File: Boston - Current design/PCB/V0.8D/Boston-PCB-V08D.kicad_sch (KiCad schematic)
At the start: 596 parts, among them J701 Conn_01x04_MountingPin, J702 Conn_01x03, J705 Conn_01x04_MountingPin, J706 Conn_ARM_JTAG_SWD_10, Q701 DTC123J, Q702 AO4406AL, SW1 MXSwitch, SW10 MXSwitch, SW100 MXSwitch, SW101 MXSwitch, SW102 MXSwitch, SW103 MXSwitch, SW104 MXSwitch, SW105-1 MXSwitch, SW105-2 MXSwitch, SW106 MXSwitch, SW107 MXSwitch, SW108 MXSwitch, SW109 MXSwitch, SW11 MXSwitch, SW110 MXSwitch, SW111 MXSwitch, SW112 MXSwitch, SW113 MXSwitch, SW114 MXSwitch, SW115 MXSwitch, SW116 MXSwitch, SW117 MXSwitch, SW118 MXSwitch, SW119 MXSwitch, SW12 MXSwitch, SW120 MXSwitch, SW121 MXSwitch, SW122 MXSwitch, SW123 MXSwitch, SW124-1 MXSwitch, SW124-2 MXSwitch, SW125 MXSwitch, SW126 Rotary_Encoder_Switch_Chassis, SW127 MXSwitch, SW128 MXSwitch, SW129 MXSwitch, SW13 MXSwitch, SW14 MXSwitch, SW15 MXSwitch, SW16 MXSwitch, SW17 MXSwitch, SW18 MXSwitch, SW19 MXSwitch, SW2 MXSwitch, SW20-1 MXSwitch, SW20-2 MXSwitch, SW200 SW_Push, SW21 MXSwitch, SW22 MXSwitch, SW23 MXSwitch, SW24 MXSwitch, SW25 MXSwitch, SW26 MXSwitch, SW27 MXSwitch, SW28 MXSwitch, SW29 MXSwitch, SW3 MXSwitch, SW30 MXSwitch, SW31 MXSwitch, SW32 MXSwitch, SW33 MXSwitch, SW34 MXSwitch, SW35 MXSwitch, SW36 MXSwitch, SW37 MXSwitch, SW38 MXSwitch, SW39-1 MXSwitch, SW39-2 MXSwitch, SW39-3 MXSwitch, SW4-1 MXSwitch, SW4-2 MXSwitch, SW40 MXSwitch, SW41 MXSwitch, SW42 MXSwitch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

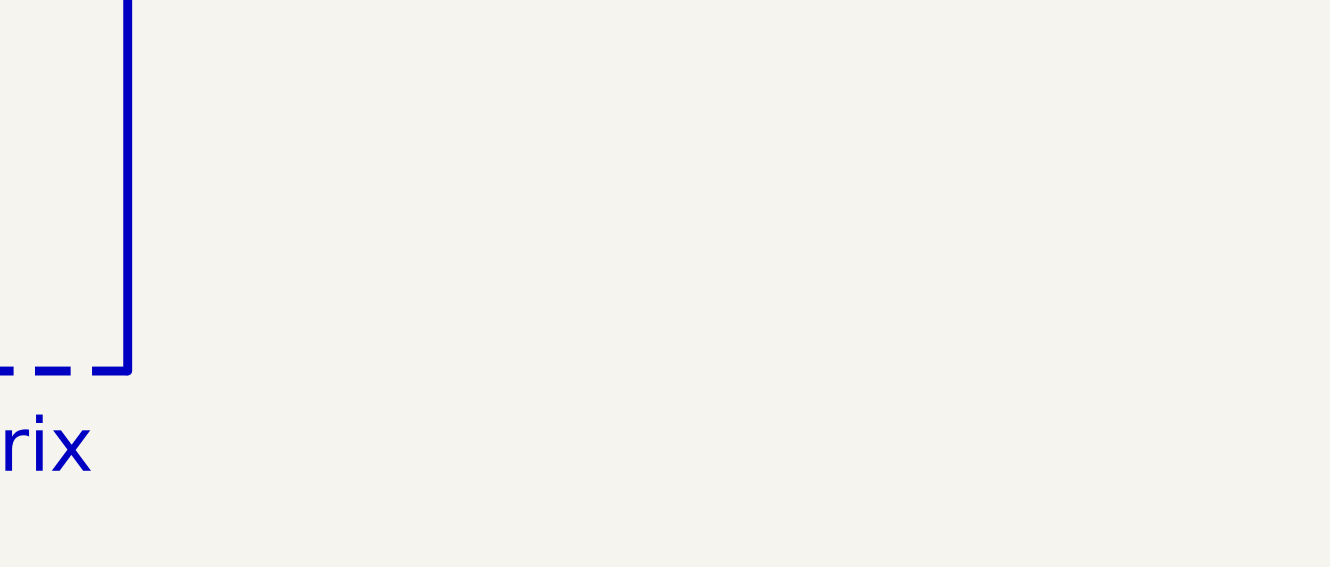
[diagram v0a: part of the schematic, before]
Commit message: Added note that SW123 and SW124-2 were accidentally swapped in the PCB layout
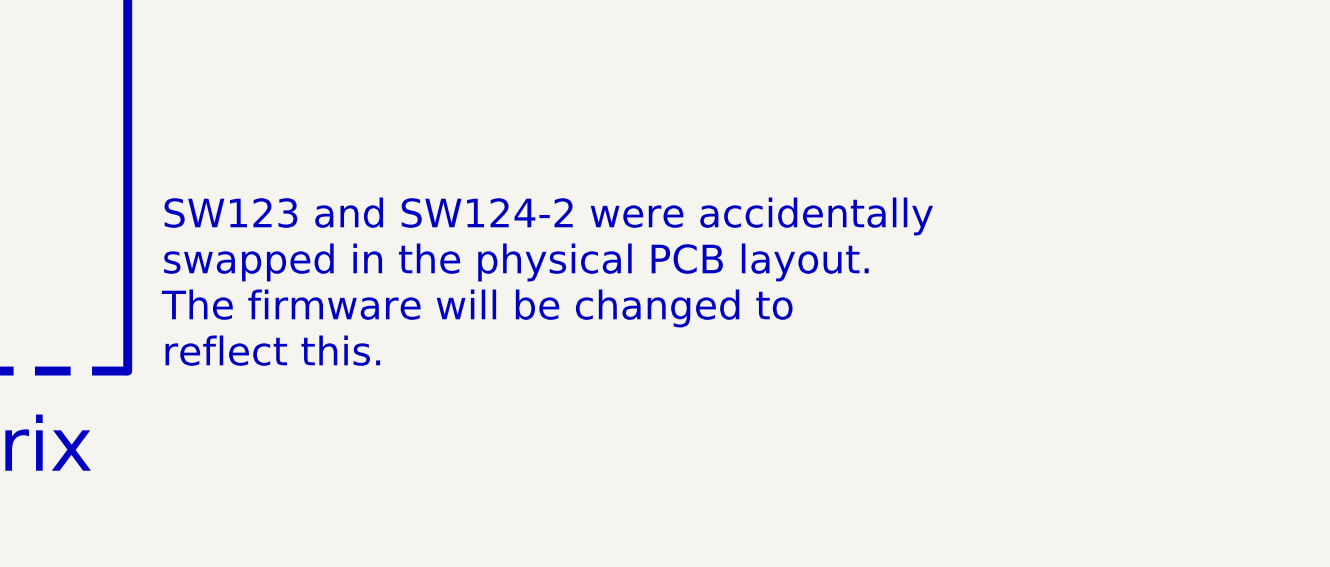
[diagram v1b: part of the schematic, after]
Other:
- note added: "SW123 and SW124-2 were accidentally swapped in the physical PCB layout. The firmware will be changed to reflect this."
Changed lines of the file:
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@@
     (effects (font (size 1.2 1.2)) (justify left bottom))
+  )
+  (text "SW123 and SW124-2 were accidentally \nswapped in the physical PCB layout. \nThe firmware will be changed to \nreflect this."
+    (at 694.69 254 0)
+    (effects (font (size 3.175 3.175)) (justify left bottom))
   )
   (text "RCtrl (1u)" (at 430.53 233.68 0)
